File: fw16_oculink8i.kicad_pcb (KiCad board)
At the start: 4 copper layers, 118.7 x 72.5 mm, 25 parts, among them J1 FXBeam, J2 Fan0, J3 Fan1, J4 173162-0131, U1 BR24G32FVT-3GE2

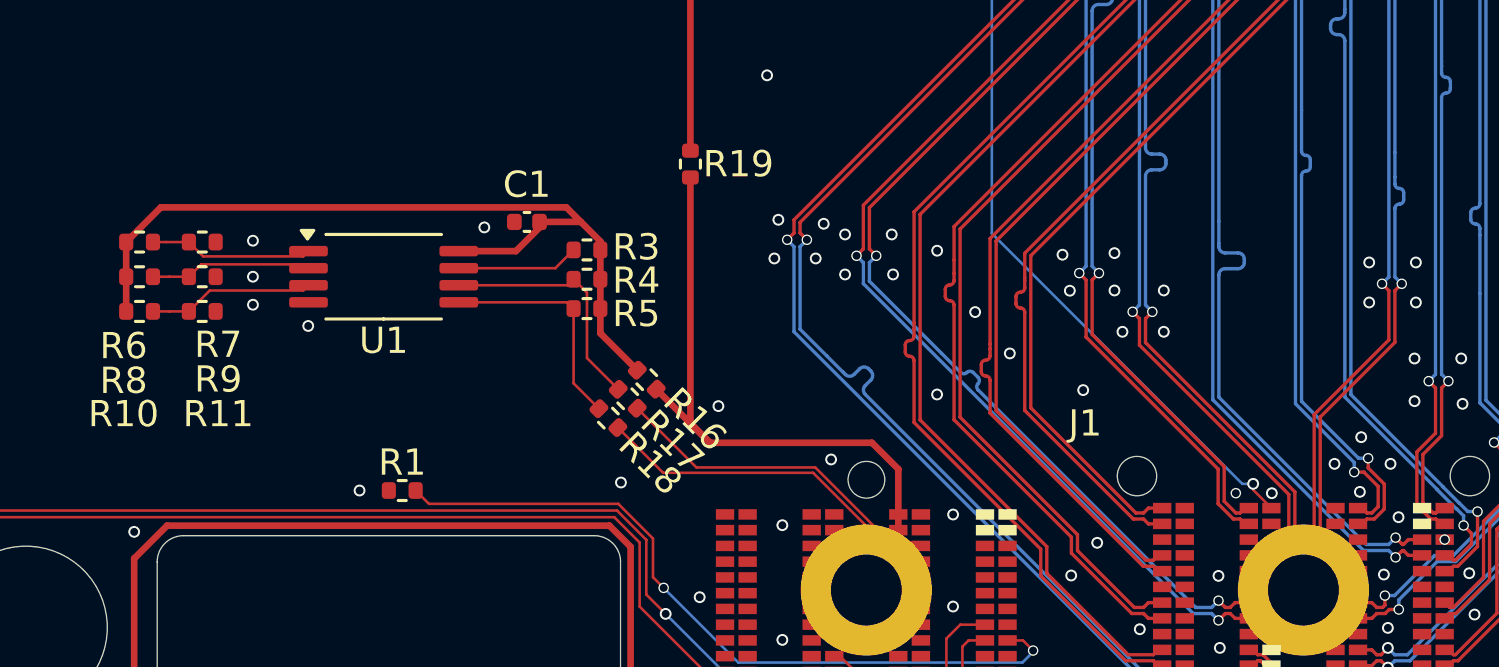
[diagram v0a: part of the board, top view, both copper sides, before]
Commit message: Add CLKREQ trace and GND EEPROM WP resistor
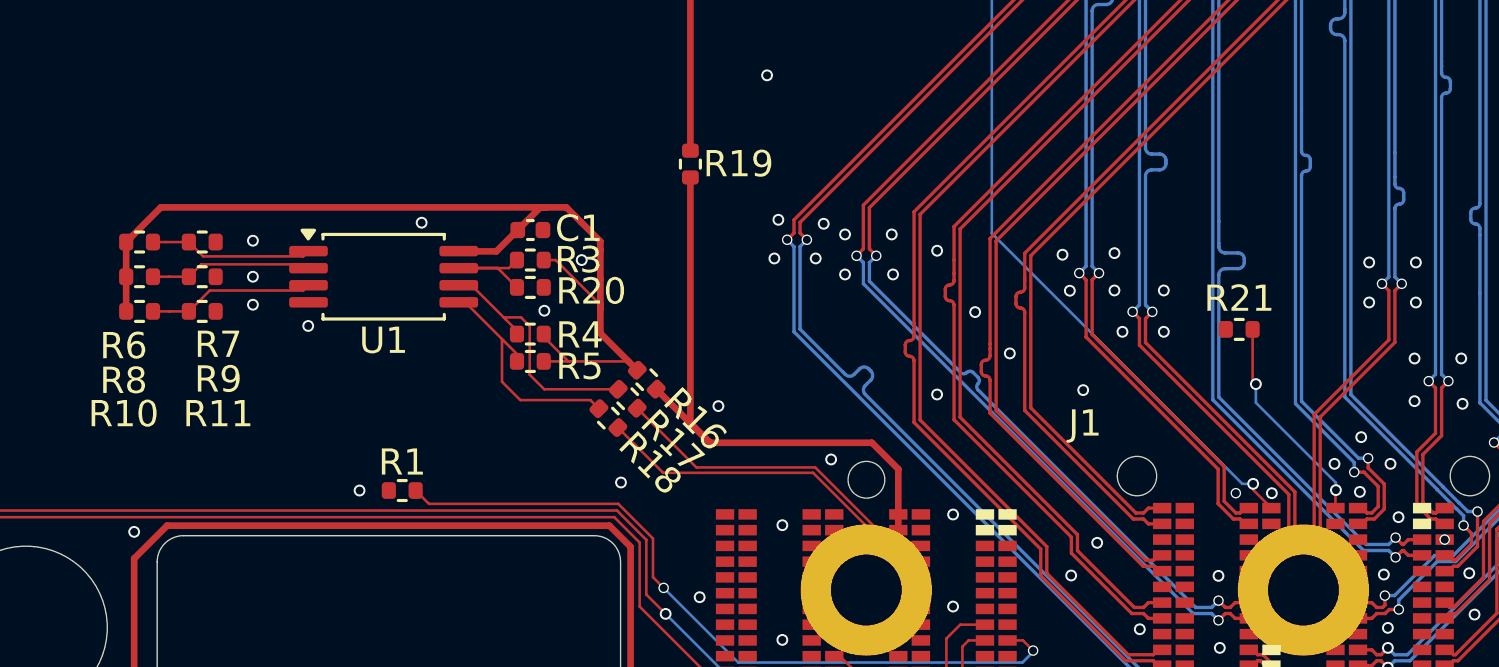
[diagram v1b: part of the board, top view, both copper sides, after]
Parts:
- added R20: 0R, Resistor_SMD:R_0402_1005Metric, F.Cu at (86.8, 79.7)
- added R21: 0R, Resistor_SMD:R_0402_1005Metric, F.Cu at (113.8, 81.3)
- moved R4 3.00 mm to (86.8, 81.5)
- moved R5 2.95 mm to (86.8, 82.5)
- moved R3 2.19 mm to (86.8, 78.7), turned to 0 degrees
- moved C1 0.34 mm to (86.8, 77.5), turned to 0 degrees
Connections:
- J1 pad SA4: unconnected-(J1-PEX_CLK_REQ#-PadSA4) -> /CLKREQ
- R3 pad 1: /3V3_EEPROM -> /EEPROM_WP
- R3 pad 2: Net-(U1-WP) -> /3V3_EEPROM
- U1 pad 7: Net-(U1-WP) -> /EEPROM_WP
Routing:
- net /CLKREQ: track 0.00 -> 8.13 mm, vias 0 -> 2
- net /3V3_EEPROM: track 32.5 -> 38.8 mm
- net /EEPROM_WP: track 0.00 -> 4.85 mm
- net Net-(U1-WP): track 4.66 -> 0.00 mm
- net Net-(U1-SDA): track 8.68 -> 9.22 mm
- net GND: vias 142 -> 144

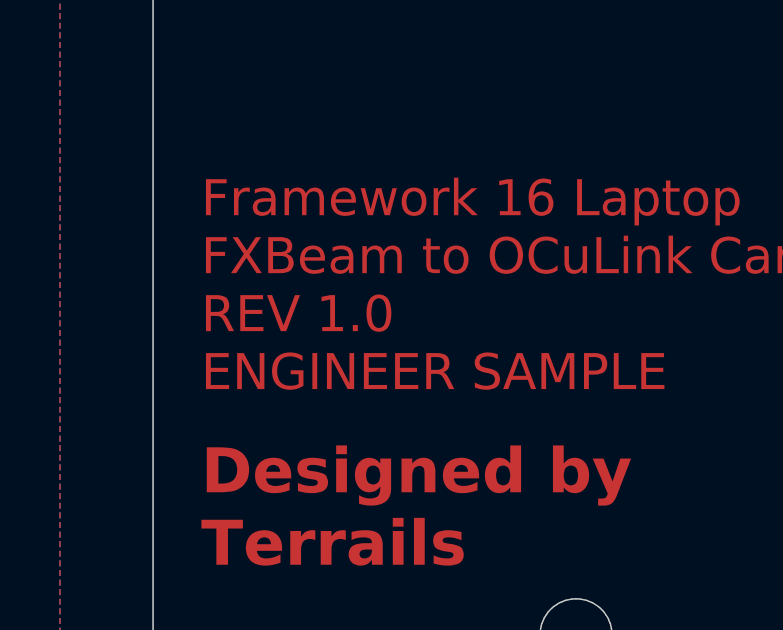
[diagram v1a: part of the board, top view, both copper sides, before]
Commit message: Update to rev 1.1 due to CLKREQ and EEPROM WP updates
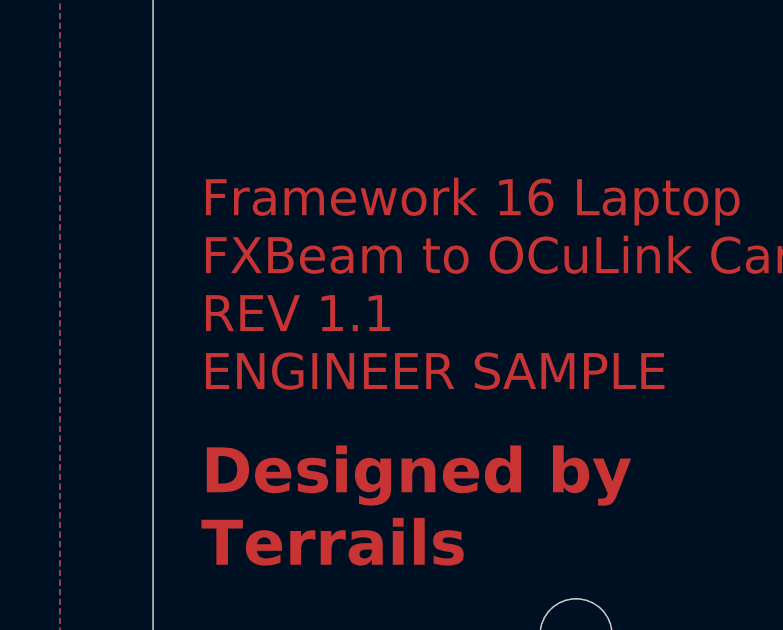
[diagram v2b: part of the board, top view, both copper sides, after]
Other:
- board text added: "Framework 16 Laptop FXBeam to OCuLink Card REV 1.1 ENGINEER SAMPLE"
- board text removed: "Framework 16 Laptop FXBeam to OCuLink Card REV 1.0 ENGINEER SAMPLE"
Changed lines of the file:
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@@
 		(layer "Edge.Cuts")
 	)
-	(gr_text "Framework 16 Laptop\nFXBeam to OCuLink Card\nREV 1.0\nENGINEER SAMPLE"
+	(gr_text "Framework 16 Laptop\nFXBeam to OCuLink Card\nREV 1.1\nENGINEER SAMPLE"
 		(at 44.704 79.516967 0)
 		(layer "F.Cu")
